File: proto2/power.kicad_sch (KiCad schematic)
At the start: 26 parts, among them U13 NCP59300

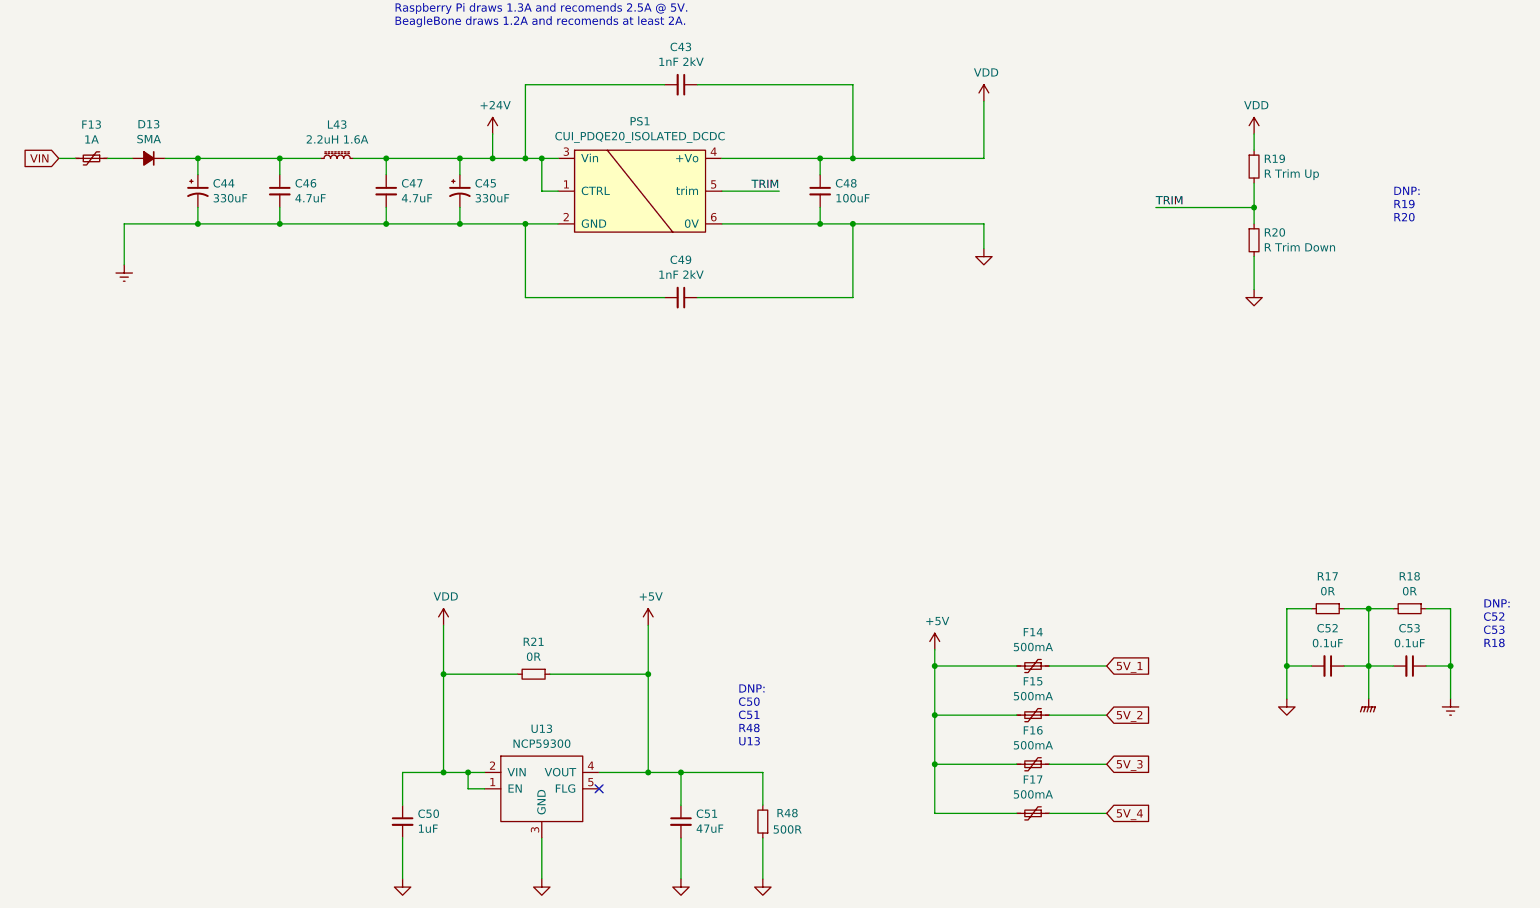
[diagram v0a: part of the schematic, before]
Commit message: Added another 2 outputs and re-routed board.
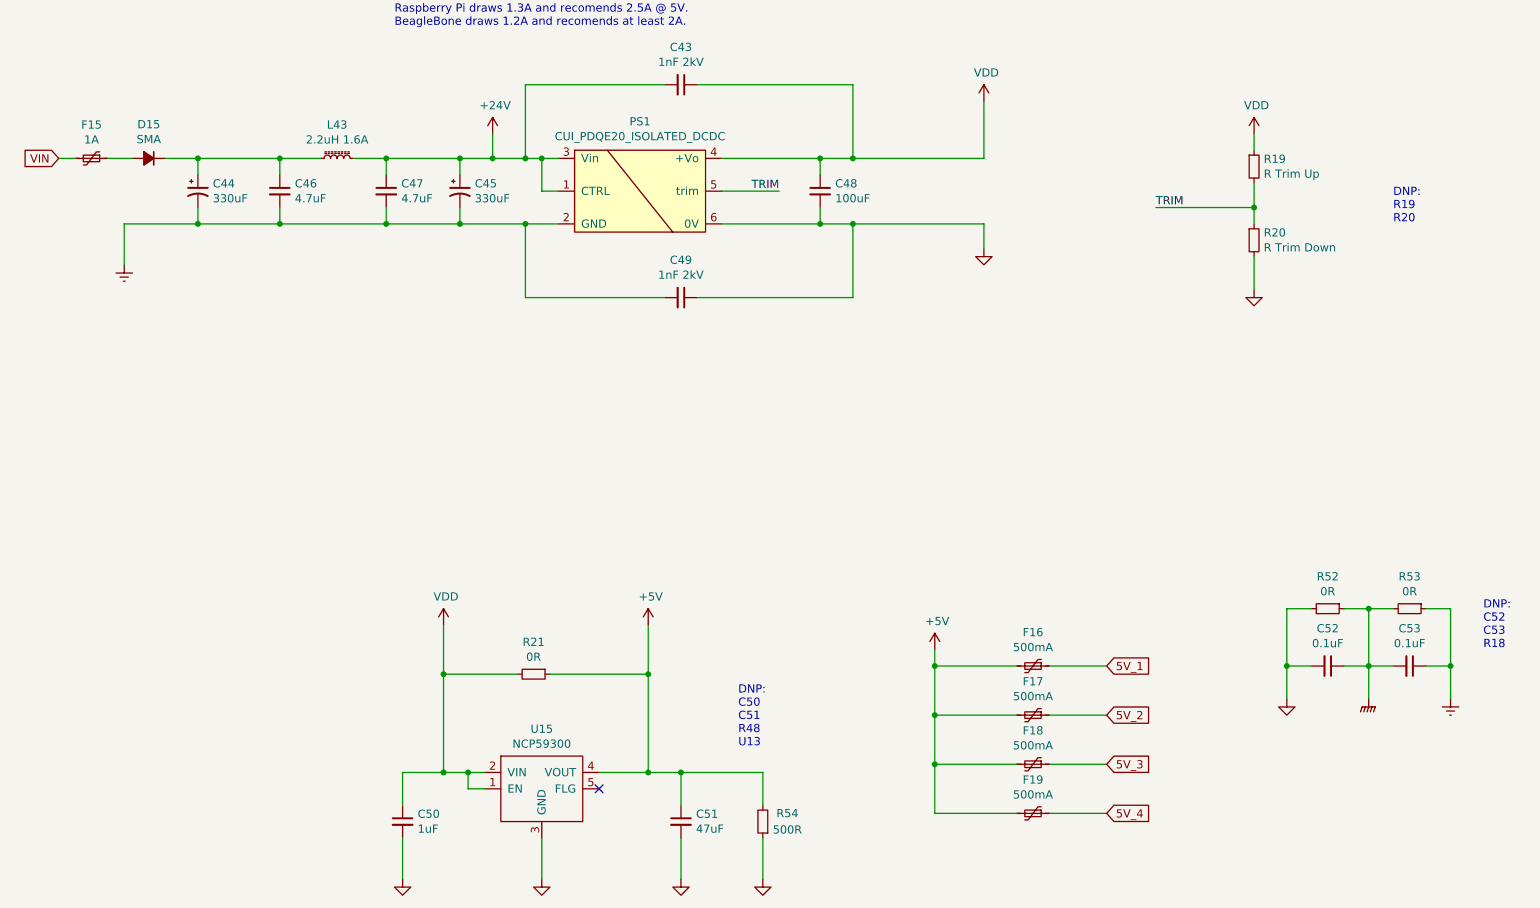
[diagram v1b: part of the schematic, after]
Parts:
- renumbered D13 to D15, F13 to F15, F14 to F16, F15 to F17, F16 to F18, F17 to F19, R17 to R52, R18 to R53, R48 to R54, U13 to U15
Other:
- title: IOB Motherboard -> Greenhouse 2.0 IO Board
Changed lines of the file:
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@@
   (paper "USLetter")
   (title_block
-    (title "IOB Motherboard")
-    (date "2021-12-14")
+    (title "Greenhouse 2.0 IO Board")
+    (date "2022-01-20")
+    (rev "0.1.1")
     (company "Langhe Greenhaus")
   )
@@
   (symbol (lib_id "Device:Polyfuse_Small") (at 30.48 44.45 270) (unit 1)
     (in_bom yes) (on_board yes)
-    (property "Reference" "F13" (id 0) (at 30.48 39.243 90))
+    (property "Reference" "F15" (id 0) (at 30.48 39.243 90))
     (property "Value" "1A" (id 1) (at 30.48 41.5544 90))
     (property "Footprint" "Resistor_SMD:R_1206_3216Metric" (id 2) (at 25.4 45.72 0)
@@
   (symbol (lib_id "Device:Polyfuse_Small") (at 176.53 146.05 270) (unit 1)
     (in_bom yes) (on_board yes)
-    (property "Reference" "F17" (id 0) (at 176.53 140.843 90))
+    (property "Reference" "F19" (id 0) (at 176.53 140.843 90))
     (property "Value" "500mA" (id 1) (at 176.53 143.1544 90))
     (property "Footprint" "Resistor_SMD:R_0805_2012Metric" (id 2) (at 171.45 147.32 0)
@@
   (symbol (lib_id "Device:Polyfuse_Small") (at 176.53 138.43 270) (unit 1)
     (in_bom yes) (on_board yes)
-    (property "Reference" "F16" (id 0) (at 176.53 133.223 90))
+    (property "Reference" "F18" (id 0) (at 176.53 133.223 90))
     (property "Value" "500mA" (id 1) (at 176.53 135.5344 90))
     (property "Footprint" "Resistor_SMD:R_0805_2012Metric" (id 2) (at 171.45 139.7 0)
@@
   (symbol (lib_id "Device:Polyfuse_Small") (at 176.53 123.19 270) (unit 1)
     (in_bom yes) (on_board yes)
-    (property "Reference" "F14" (id 0) (at 176.53 117.983 90))
+    (property "Reference" "F16" (id 0) (at 176.53 117.983 90))
     (property "Value" "500mA" (id 1) (at 176.53 120.2944 90))
     (property "Footprint" "Resistor_SMD:R_0805_2012Metric" (id 2) (at 171.45 124.46 0)
@@
   (symbol (lib_id "Device:Polyfuse_Small") (at 176.53 130.81 270) (unit 1)
     (in_bom yes) (on_board yes)
-    (property "Reference" "F15" (id 0) (at 176.53 125.603 90))
+    (property "Reference" "F17" (id 0) (at 176.53 125.603 90))
     (property "Value" "500mA" (id 1) (at 176.53 127.9144 90))
     (property "Footprint" "Resistor_SMD:R_0805_2012Metric" (id 2) (at 171.45 132.08 0)
@@
   (symbol (lib_id "BCR:NCP59300") (at 100.33 147.32 0) (unit 1)
     (in_bom yes) (on_board yes)
-    (property "Reference" "U13" (id 0) (at 100.33 132.969 0))
+    (property "Reference" "U15" (id 0) (at 100.33 132.969 0))
     (property "Value" "NCP59300" (id 1) (at 100.33 135.2804 0))
     (property "Footprint" "Package_TO_SOT_SMD:TO-263-5_TabPin3" (id 2) (at 100.33 147.32 0)
@@
   (symbol (lib_id "Device:R_Small") (at 222.25 114.3 270) (unit 1)
     (in_bom yes) (on_board yes)
-    (property "Reference" "R17" (id 0) (at 222.25 109.3216 90))
+    (property "Reference" "R52" (id 0) (at 222.25 109.3216 90))
     (property "Value" "0R" (id 1) (at 222.25 111.633 90))
     (property "Footprint" "Resistor_SMD:R_0805_2012Metric" (id 2) (at 222.25 114.3 0)
@@
   (symbol (lib_id "Device:R_Small") (at 234.95 114.3 270) (unit 1)
     (in_bom yes) (on_board yes)
-    (property "Reference" "R18" (id 0) (at 234.95 109.3216 90))
+    (property "Reference" "R53" (id 0) (at 234.95 109.3216 90))
     (property "Value" "0R" (id 1) (at 234.95 111.633 90))
     (property "Footprint" "Resistor_SMD:R_0805_2012Metric" (id 2) (at 234.95 114.3 0)
@@
   (symbol (lib_id "Device:R_Small") (at 134.62 147.32 180) (unit 1)
     (in_bom yes) (on_board yes)
-    (property "Reference" "R48" (id 0) (at 138.43 146.05 0))
+    (property "Reference" "R54" (id 0) (at 138.43 146.05 0))
     (property "Value" "500R" (id 1) (at 138.43 148.59 0))
     (property "Footprint" "Capacitor_SMD:C_0805_2012Metric" (id 2) (at 134.62 147.32 0)
@@
   (symbol (lib_id "Device:D_Small_ALT") (at 39.37 44.45 180) (unit 1)
     (in_bom yes) (on_board yes)
-    (property "Reference" "D13" (id 0) (at 39.37 39.1922 0))
+    (property "Reference" "D15" (id 0) (at 39.37 39.1922 0))
     (property "Value" "SMA" (id 1) (at 39.37 41.5036 0))
     (property "Footprint" "Diode_SMD:D_SOD-123F" (id 2) (at 39.37 44.45 90)

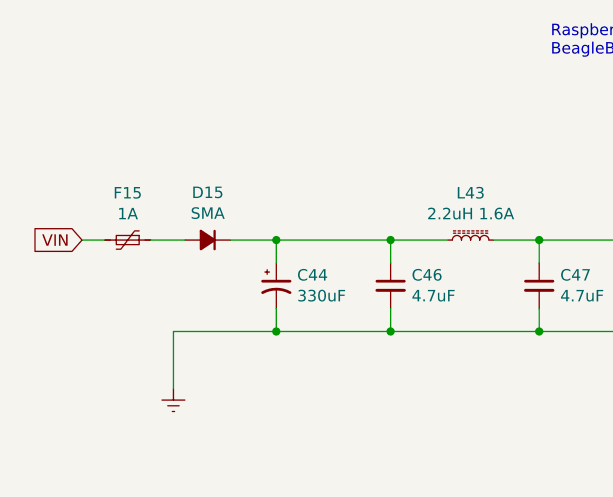
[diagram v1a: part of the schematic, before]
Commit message: Added Datasheet links
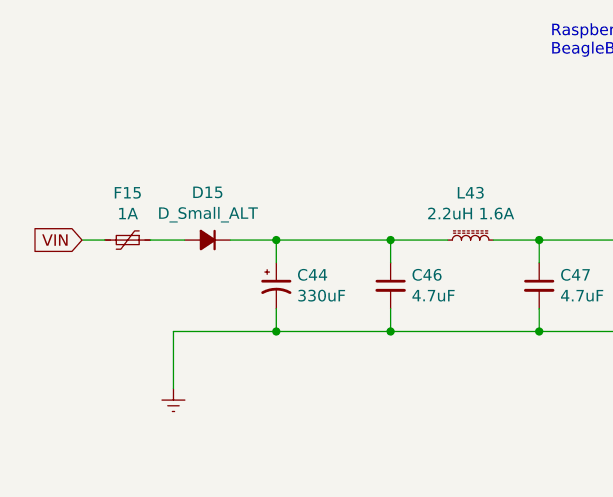
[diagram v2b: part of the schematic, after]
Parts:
- D15: value SMA -> D_Small_ALT; Manufacturer (none) -> MDD; Part Number (none) -> SM4007PL
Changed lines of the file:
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@@
       (effects (font (size 1.27 1.27)) hide)
     )
-    (property "Datasheet" "~" (id 3) (at 68.58 44.45 0)
+    (property "Datasheet" "https://datasheet.lcsc.com/lcsc/1810250922_Murata-Electronics-LQH32PN2R2NN0L_C86074.pdf" (id 3) (at 68.58 44.45 0)
       (effects (font (size 1.27 1.27)) hide)
     )
@@
       (effects (font (size 1.27 1.27)) hide)
     )
-    (property "Datasheet" "~" (id 3) (at 143.51 49.53 0)
+    (property "Datasheet" "https://datasheet.lcsc.com/lcsc/1811061115_Murata-Electronics-GRM31CR61A107ME05L_C312983.pdf" (id 3) (at 143.51 49.53 0)
       (effects (font (size 1.27 1.27)) hide)
     )
@@
       (effects (font (size 1.27 1.27)) hide)
     )
-    (property "Datasheet" "~" (id 3) (at 121.92 33.02 0)
+    (property "Datasheet" "https://datasheet.lcsc.com/lcsc/1810311314_FH-Guangdong-Fenghua-Advanced-Tech-1206B102K202NT_C9196.pdf" (id 3) (at 121.92 33.02 0)
       (effects (font (size 1.27 1.27)) hide)
     )
@@
       (effects (font (size 1.27 1.27)) hide)
     )
-    (property "Datasheet" "~" (id 3) (at 121.92 66.04 0)
+    (property "Datasheet" "https://datasheet.lcsc.com/lcsc/1810311314_FH-Guangdong-Fenghua-Advanced-Tech-1206B102K202NT_C9196.pdf" (id 3) (at 121.92 66.04 0)
       (effects (font (size 1.27 1.27)) hide)
     )
@@
       (effects (font (size 1.27 1.27)) hide)
     )
-    (property "Datasheet" "~" (id 3) (at 46.99 49.53 0)
+    (property "Datasheet" "https://datasheet.lcsc.com/lcsc/1810261813_Honor-Elec-VT1H331M1213_C94443.pdf" (id 3) (at 46.99 49.53 0)
       (effects (font (size 1.27 1.27)) hide)
     )
@@
       (effects (font (size 1.27 1.27)) hide)
     )
-    (property "Datasheet" "~" (id 3) (at 87.63 49.53 0)
+    (property "Datasheet" "https://datasheet.lcsc.com/lcsc/1810261813_Honor-Elec-VT1H331M1213_C94443.pdf" (id 3) (at 87.63 49.53 0)
       (effects (font (size 1.27 1.27)) hide)
     )
@@
       (effects (font (size 1.27 1.27)) hide)
     )
-    (property "Datasheet" "~" (id 3) (at 76.2 49.53 0)
+    (property "Datasheet" "https://datasheet.lcsc.com/lcsc/2004251506_Murata-Electronics-GRM21BR61H106KE43L_C440198.pdf" (id 3) (at 76.2 49.53 0)
       (effects (font (size 1.27 1.27)) hide)
     )
@@
       (effects (font (size 1.27 1.27)) hide)
     )
-    (property "Datasheet" "~" (id 3) (at 59.69 49.53 0)
+    (property "Datasheet" "https://datasheet.lcsc.com/lcsc/2004251506_Murata-Electronics-GRM21BR61H106KE43L_C440198.pdf" (id 3) (at 59.69 49.53 0)
       (effects (font (size 1.27 1.27)) hide)
     )
@@
       (effects (font (size 1.27 1.27)) hide)
     )
-    (property "Datasheet" "~" (id 3) (at 99.06 124.46 0)
+    (property "Datasheet" "https://datasheet.lcsc.com/lcsc/2110251930_UNI-ROYAL-Uniroyal-Elec-1206W4F0000T5E_C17888.pdf" (id 3) (at 99.06 124.46 0)
       (effects (font (size 1.27 1.27)) hide)
     )
@@
       (effects (font (size 1.27 1.27)) (justify left) hide)
     )
-    (property "Datasheet" "~" (id 3) (at 30.48 44.45 0)
+    (property "Datasheet" "https://datasheet.lcsc.com/lcsc/1809211126_TECHFUSE-nSMD050-33V_C70077.pdf" (id 3) (at 30.48 44.45 0)
       (effects (font (size 1.27 1.27)) hide)
     )
@@
       (effects (font (size 1.27 1.27)) (justify left) hide)
     )
-    (property "Datasheet" "~" (id 3) (at 176.53 146.05 0)
+    (property "Datasheet" "https://datasheet.lcsc.com/lcsc/1809271532_TECHFUSE-SMD0805-020-16V_C70057.pdf" (id 3) (at 176.53 146.05 0)
       (effects (font (size 1.27 1.27)) hide)
     )
@@
       (effects (font (size 1.27 1.27)) (justify left) hide)
     )
-    (property "Datasheet" "~" (id 3) (at 176.53 138.43 0)
+    (property "Datasheet" "https://datasheet.lcsc.com/lcsc/1809271532_TECHFUSE-SMD0805-020-16V_C70057.pdf" (id 3) (at 176.53 138.43 0)
       (effects (font (size 1.27 1.27)) hide)
     )
@@
       (effects (font (size 1.27 1.27)) (justify left) hide)
     )
-    (property "Datasheet" "~" (id 3) (at 176.53 123.19 0)
+    (property "Datasheet" "https://datasheet.lcsc.com/lcsc/1809271532_TECHFUSE-SMD0805-020-16V_C70057.pdf" (id 3) (at 176.53 123.19 0)
       (effects (font (size 1.27 1.27)) hide)
     )
@@
       (effects (font (size 1.27 1.27)) (justify left) hide)
     )
-    (property "Datasheet" "~" (id 3) (at 176.53 130.81 0)
+    (property "Datasheet" "https://datasheet.lcsc.com/lcsc/1809271532_TECHFUSE-SMD0805-020-16V_C70057.pdf" (id 3) (at 176.53 130.81 0)
       (effects (font (size 1.27 1.27)) hide)
     )
@@
       (effects (font (size 1.27 1.27)) hide)
     )
-    (property "Datasheet" "https://www.onsemi.com/pdf/datasheet/ncp59300-d.pdf" (id 3) (at 100.33 147.32 0)
+    (property "Datasheet" "~" (id 3) (at 100.33 147.32 0)
       (effects (font (size 1.27 1.27)) hide)
     )
@@
       (effects (font (size 1.27 1.27)) hide)
     )
-    (property "Datasheet" "~" (id 3) (at 222.25 114.3 0)
+    (property "Datasheet" "https://datasheet.lcsc.com/lcsc/2110251730_UNI-ROYAL-Uniroyal-Elec-0805W8F0000T5E_C17477.pdf" (id 3) (at 222.25 114.3 0)
       (effects (font (size 1.27 1.27)) hide)
     )
@@
     (in_bom yes) (on_board yes)
     (property "Reference" "D15" (id 0) (at 39.37 39.1922 0))
-    (property "Value" "SMA" (id 1) (at 39.37 41.5036 0))
+    (property "Value" "D_Small_ALT" (id 1) (at 39.37 41.5036 0))
     (property "Footprint" "Diode_SMD:D_SOD-123F" (id 2) (at 39.37 44.45 90)
       (effects (font (size 1.27 1.27)) hide)
     )
-    (property "Datasheet" "~" (id 3) (at 39.37 44.45 90)
+    (property "Datasheet" "https://datasheet.lcsc.com/lcsc/1809301215_MDD-Microdiode-Electronics--SM4007PL_C64898.pdf" (id 3) (at 39.37 44.45 90)
       (effects (font (size 1.27 1.27)) hide)
     )
@@
       (effects (font (size 1.27 1.27)) hide)
     )
+    (property "Manufacturer" "MDD" (id 5) (at 39.37 44.45 0)
+      (effects (font (size 1.27 1.27)) hide)
+    )
+    (property "Part Number" "SM4007PL" (id 6) (at 39.37 44.45 0)
+      (effects (font (size 1.27 1.27)) hide)
+    )

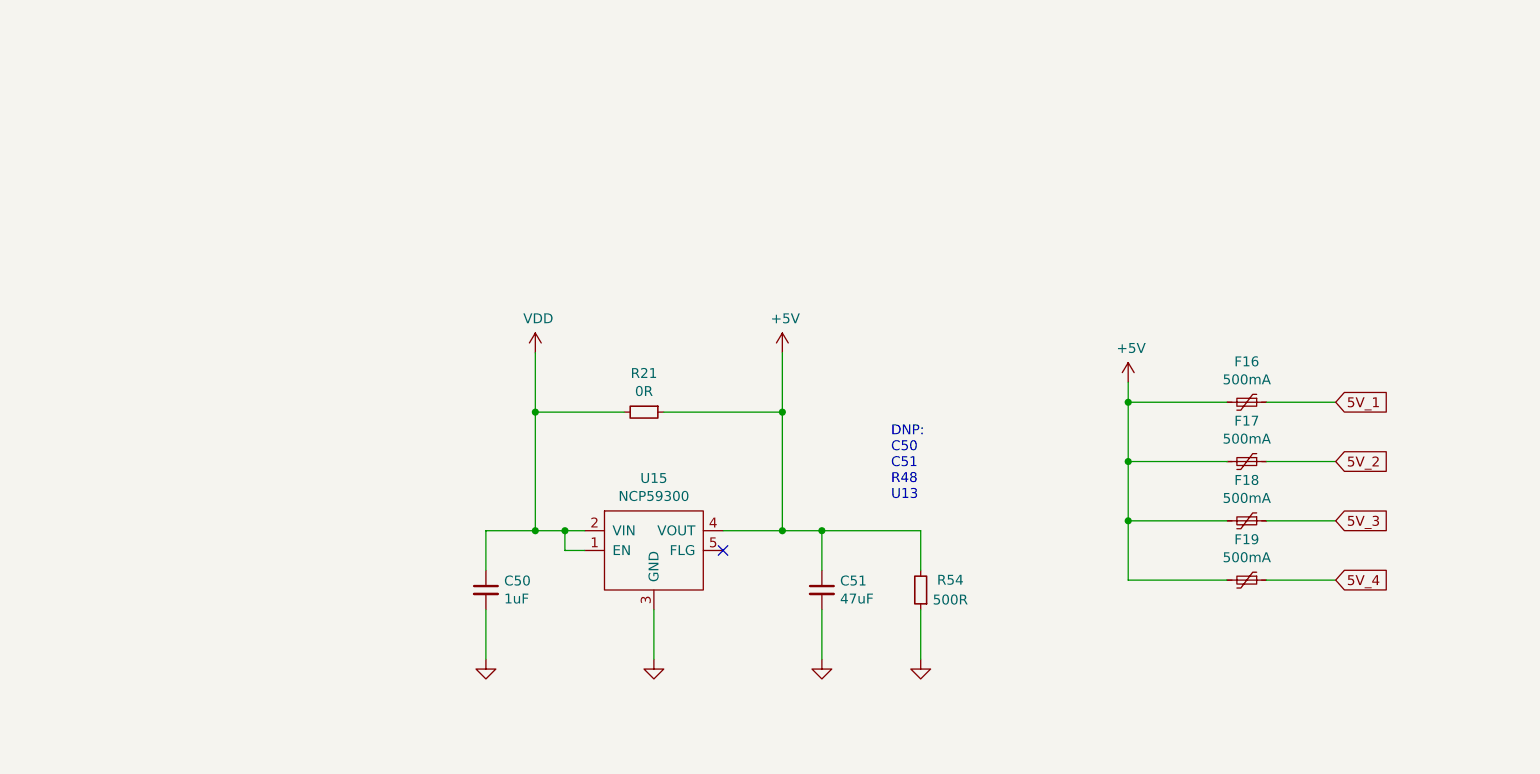
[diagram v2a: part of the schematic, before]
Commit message: Added switch for 5V external devices power based off SYS_RESETn.
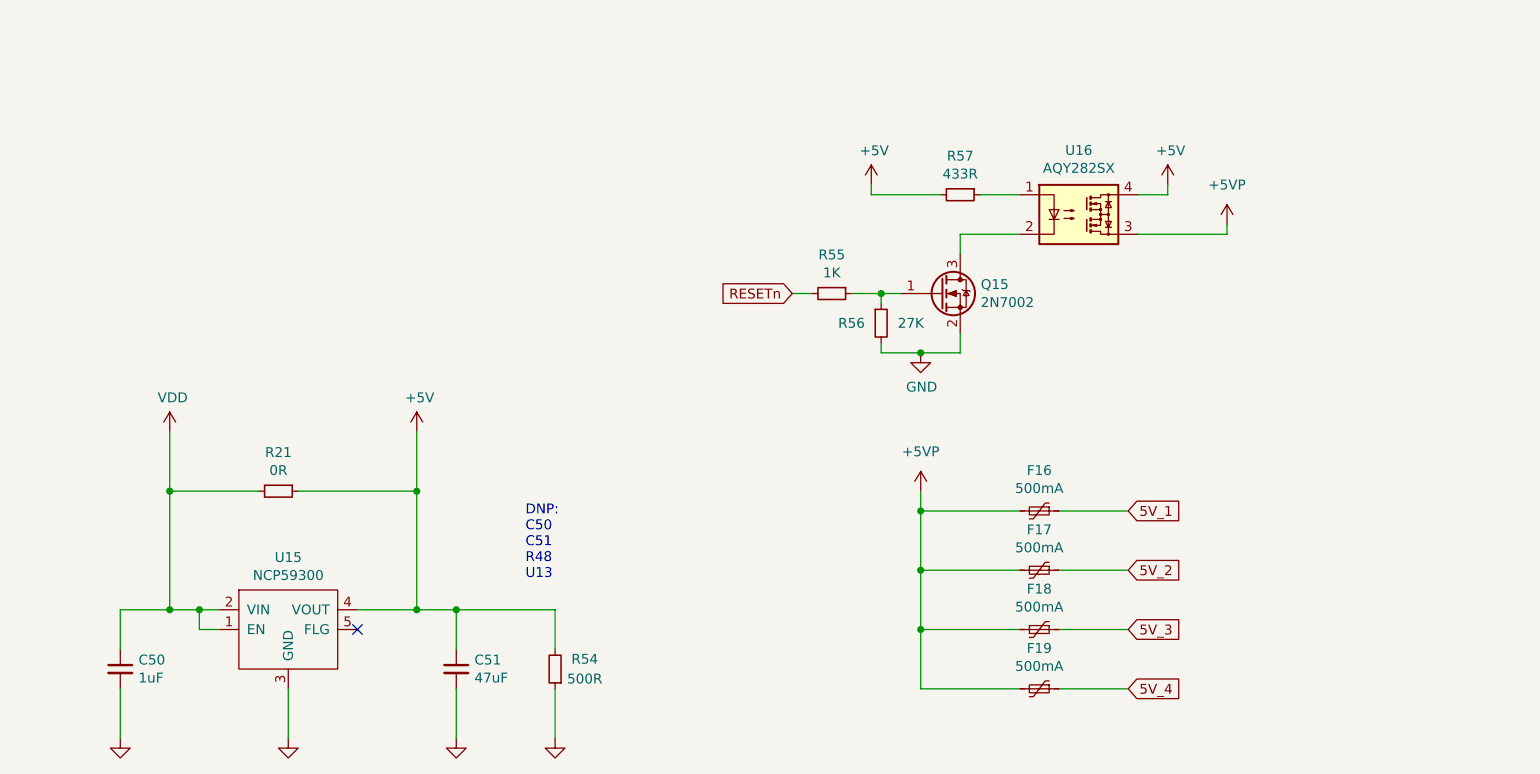
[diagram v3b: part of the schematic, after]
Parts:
- added Q15: 2N7002, Package_TO_SOT_SMD:SOT-23, symbol Transistor_FET:2N7002
- added R55: 1K, Resistor_SMD:R_0805_2012Metric, symbol Device:R_Small
- added R56: 27K, Resistor_SMD:R_0805_2012Metric, symbol Device:R_Small
- added R57: 433R, Resistor_SMD:R_0805_2012Metric, symbol Device:R_Small
- added U16: AQY282SX, Package_SO:SO-4_4.4x4.3mm_P2.54mm, symbol Relay_SolidState:ASSR-1218
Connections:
- net +5V: now also R57.2, U16.4; no longer F16.2, F17.2, F18.2, F19.2
- net GND: now also Q15.2 (S), R56.2
- new net: Q15.1 (G), R55.1, R56.1
- new net: Q15.3 (D), U16.2
- new net: R57.1, U16.1
- new net +5VP: F16.2, F17.2, F18.2, F19.2, U16.3
- new net RESETn: R55.2
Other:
- moved on the sheet: C50, C51, F16, F17, F18, F19, R21, R54, U15
